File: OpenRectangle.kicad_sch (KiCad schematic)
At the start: 84 parts, among them J1 USB C Connector, J2 JTAG_TC2030, SW1 MX_SW_HS, SW10 MX_SW_HS, SW11 MX_SW_HS, SW12 MX_SW_solder, SW13 MX_SW_HS, SW14 MX_SW_solder, SW15 MX_SW_solder, SW16 MX_SW_HS, SW17 MX_SW_HS, SW18 MX_SW_solder, SW19 MX_SW_HS, SW2 MX_SW_solder, SW20 MX_SW_solder, SW21 MX_SW_solder, SW22 MX_SW_HS, SW23 MX_SW_HS, SW24 MX_SW_solder, SW25 MX_SW_solder, SW26 MX_SW_HS, SW27 MX_SW_solder, SW28 MX_SW_HS, SW29 MX_SW_HS, SW3 MX_SW_HS, SW30 MX_SW_solder, SW31 MX_SW_solder, SW32 MX_SW_HS, SW33 MX_SW_solder, SW34 MX_SW_HS, SW35 MX_SW_HS, SW36 MX_SW_solder, SW37 MX_SW_solder, SW38 MX_SW_HS, SW39 MX_SW_HS, SW4 MX_SW_solder, SW40 MX_SW_solder, SW41 Boot, SW5 MX_SW_HS, SW6 MX_SW_solder, SW7 MX_SW_HS, SW8 MX_SW_solder, SW9 MX_SW_solder, U1 XC6206, U2 USBLC6-2SC6, U3 RP2040, U4 W25Q128JVS, Y1 12MHz

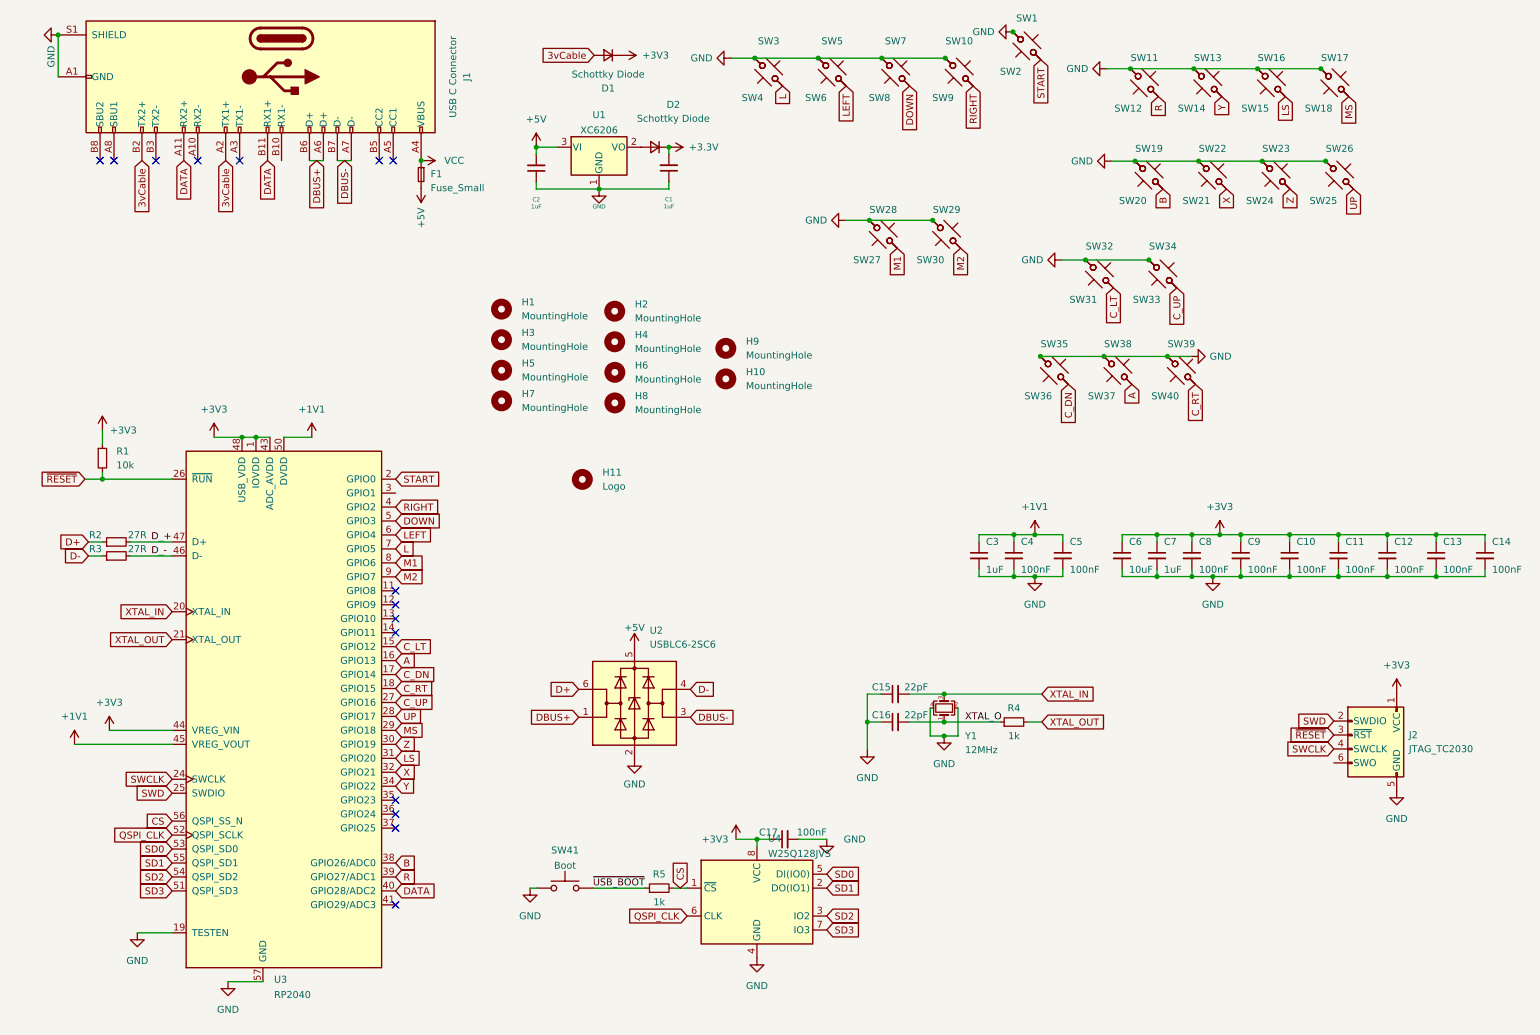
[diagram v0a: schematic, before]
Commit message: Updates version
Added:
- C to C functionality
- VBUS sensing
- Green LED
- Shield connected to GND via a resistor
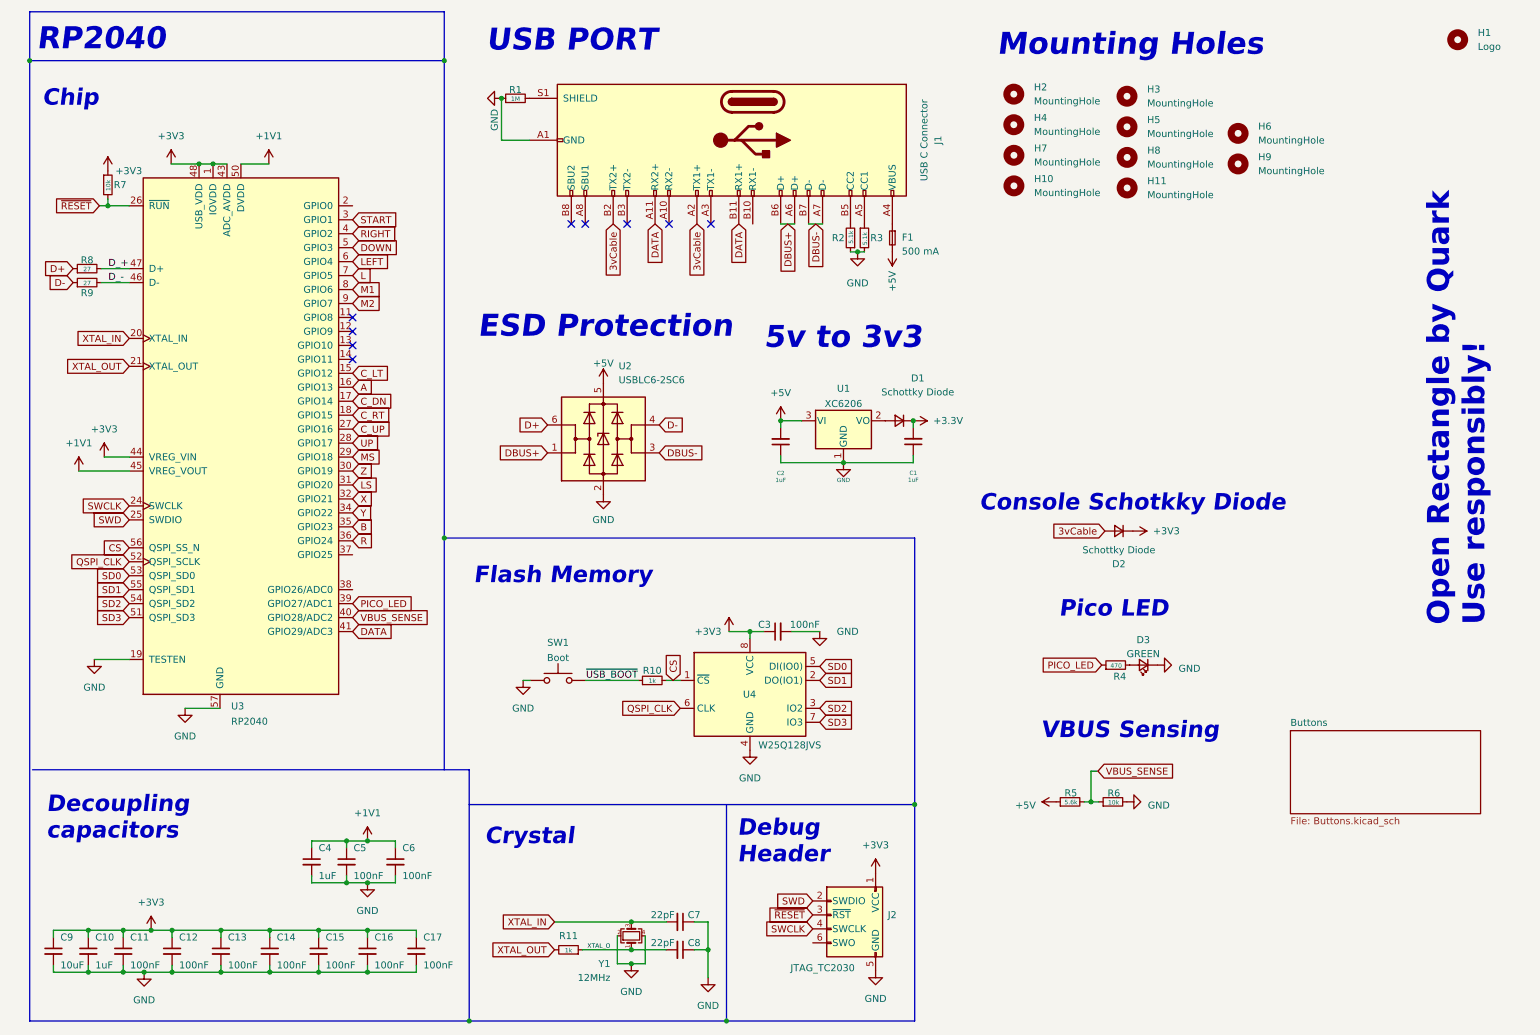
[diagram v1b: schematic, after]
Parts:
- removed SW1, SW10, SW11, SW13, SW16, SW17, SW19, SW22, SW23, SW26, SW28, SW29, SW3, SW32, SW34, SW35, SW38, SW39, SW5, SW7: MX_SW_HS, marbastlib-mx:SW_MX_HS_1u, symbol marbastlib-mx:MX_SW_HS
- removed SW12, SW14, SW15, SW18, SW2, SW20, SW21, SW24, SW25, SW27, SW30, SW31, SW33, SW36, SW37, SW4, SW40, SW6, SW8, SW9: MX_SW_solder, marbastlib-mx:SW_MX_1u, symbol marbastlib-mx:MX_SW_solder
- added D3: GREEN, LED_SMD:LED_0805_2012Metric, symbol Device:LED_Small
- added R1: 1M, Resistor_SMD:R_0603_1608Metric, symbol Device:R_Small
- added R2, R3: 5.1k, Resistor_SMD:R_0402_1005Metric, symbol Device:R_Small
- added R4: 470, Resistor_SMD:R_0402_1005Metric, symbol Device:R_Small
- added R5: 5.6k, Resistor_SMD:R_0603_1608Metric, symbol Device:R_Small
- added R6: 10k, Resistor_SMD:R_0603_1608Metric, symbol Device:R_Small
- F1: value Fuse_Small -> 500 mA
- R8: renamed from R2; value 27R -> 27
- R9: renamed from R3; value 27R -> 27
- renumbered C7 to C10, C8 to C11, C9 to C12, C10 to C13, C11 to C14, C12 to C15, C13 to C16, C14 to C17, C17 to C3, C3 to C4, C4 to C5, C5 to C6, C15 to C7, C16 to C8, C6 to C9, D2 to D1, D1 to D2, H11 to H1, H7 to H10, H8 to H11, H1 to H2, H2 to H3, H3 to H4, H4 to H5, H9 to H6, H5 to H7, H6 to H8, H10 to H9, R5 to R10, R4 to R11, R1 to R7, SW41 to SW1
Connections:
- net +5V: now also R5.1
- net B: now also U3.35 (GPIO23); no longer U3.38 (GPIO26/ADC0)
- net DATA: now also U3.41 (GPIO29/ADC3); no longer U3.40 (GPIO28/ADC2)
- net GND: now also D3.1 (K), R1.1, R2.1, R3.2, R6.2; no longer J1.S1 (SHIELD)
- net R: now also U3.36 (GPIO24); no longer U3.39 (GPIO27/ADC1)
- net START: now also U3.3 (GPIO1); no longer U3.2 (GPIO0)
- net at J1.A5 (CC1): now also R3.1
- net at J1.B5 (CC2): now also R2.2
- net VCC: no longer names the net of F1.1, J1.A4 (VBUS), J1.A9 (VBUS), J1.B4 (VBUS), J1.B9 (VBUS)
- new net: D3.2 (A), R4.2
- new net: J1.S1 (SHIELD), R1.2
- new net PICO_LED: R4.1, U3.39 (GPIO27/ADC1)
- new net VBUS_SENSE: R5.2, R6.1, U3.40 (GPIO28/ADC2)
- no-connect marks 15 -> 9
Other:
- added sheet Buttons (Buttons.kicad_sch)
- note added: "5v to 3v3"
- note added: "Chip"
- note added: "Console Schotkky Diode"
- note added: "Crystal"
- note added: "Debug Header"
- note added: "Decoupling capacitors"
- note added: "ESD Protection"
- note added: "Flash Memory"
- note added: "Mounting Holes"
- note added: "Open Rectangle by Quark Use responsibly!"
- note added: "Pico LED"
- note added: "RP2040"
- note added: "USB PORT"
- note added: "VBUS Sensing"
- moved on the sheet: C1, C10, C11, C12, C13, C14, C15, C16, C17, C2, C3, C4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
